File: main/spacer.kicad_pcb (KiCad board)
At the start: 2 copper layers, 100 x 100 mm, 114 parts

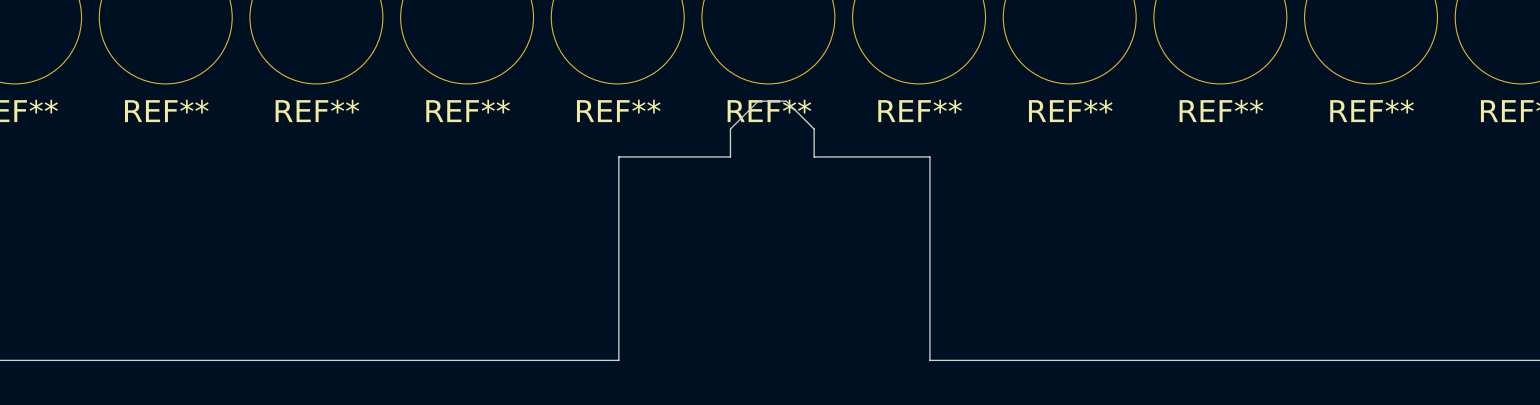
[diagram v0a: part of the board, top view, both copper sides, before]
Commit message: progress and yet not.  trying for v0.2.0, but some issues: letters not aligned, switches to tall, minute leds too close to USB_C
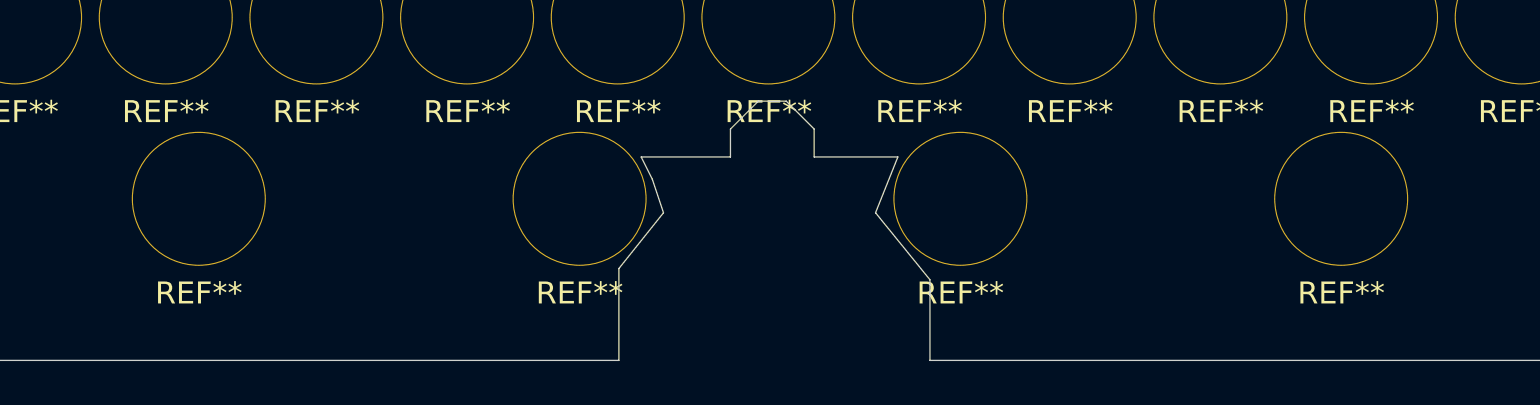
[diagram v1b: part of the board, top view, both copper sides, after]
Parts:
- added REF**: ws2812b-mini_hole, william_fab:ws2812b-mini_hole, F.Cu at (76.0, 92.6)
- added REF**: ws2812b-mini_hole, william_fab:ws2812b-mini_hole, F.Cu at (58.7, 92.6)
- added REF**: ws2812b-mini_hole, william_fab:ws2812b-mini_hole, F.Cu at (41.3, 92.6)
- added REF**: ws2812b-mini_hole, william_fab:ws2812b-mini_hole, F.Cu at (24.0, 92.6)
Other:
- outline, holes or cut-outs redrawn
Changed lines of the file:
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@@
-(kicad_pcb (version 20171130) (host pcbnew "(5.1.4)-1")
+(kicad_pcb (version 20171130) (host pcbnew "(5.1.5)-2")
   (general
     (thickness 1.6)
-    (drawings 47)
+    (drawings 52)
     (tracks 0)
     (zones 0)
-    (modules 114)
+    (modules 118)
     (nets 1)
   )
@@
       (drillshape 0)
       (scaleselection 1)
-      (outputdirectory "../fabrication/v0.2.0/"))
+      (outputdirectory "../fabrication/v0.2.0_spacer/"))
   )
   (net 0 "")
@@
   )
   (module william_fab:ws2812b-mini_hole (layer F.Cu)
+    (at 76 92.645)
+    (fp_text reference REF** (at 0 4.3) (layer F.SilkS)
+      (effects (font (size 1 1) (thickness 0.15)))
+    )
+    (fp_text value ws2812b-mini_hole (at 0.3 -6.35) (layer F.Fab)
+      (effects (font (size 1 1) (thickness 0.15)))
+    )
+    (pad 1 thru_hole circle (at 0 0) (size 6.1 6.1) (drill 6) (layers *.Cu *.Mask))
+  )
+  (module william_fab:ws2812b-mini_hole (layer F.Cu)
+    (at 58.666666 92.645)
+    (fp_text reference REF** (at 0 4.3) (layer F.SilkS)
+      (effects (font (size 1 1) (thickness 0.15)))
+    )
+    (fp_text value ws2812b-mini_hole (at 0.3 -6.35) (layer F.Fab)
+      (effects (font (size 1 1) (thickness 0.15)))
+    )
+    (pad 1 thru_hole circle (at 0 0) (size 6.1 6.1) (drill 6) (layers *.Cu *.Mask))
+  )
+  (module william_fab:ws2812b-mini_hole (layer F.Cu)
+    (at 41.333333 92.645)
+    (fp_text reference REF** (at 0 4.3) (layer F.SilkS)
+      (effects (font (size 1 1) (thickness 0.15)))
+    )
+    (fp_text value ws2812b-mini_hole (at 0.3 -6.35) (layer F.Fab)
+      (effects (font (size 1 1) (thickness 0.15)))
+    )
+    (pad 1 thru_hole circle (at 0 0) (size 6.1 6.1) (drill 6) (layers *.Cu *.Mask))
+  )
+  (module william_fab:ws2812b-mini_hole (layer F.Cu)
+    (at 24 92.645)
+    (fp_text reference REF** (at 0 4.3) (layer F.SilkS)
+      (effects (font (size 1 1) (thickness 0.15)))
+    )
+    (fp_text value ws2812b-mini_hole (at 0.3 -6.35) (layer F.Fab)
+      (effects (font (size 1 1) (thickness 0.15)))
+    )
+    (pad 1 thru_hole circle (at 0 0) (size 6.1 6.1) (drill 6) (layers *.Cu *.Mask))
+  )
+  (module william_fab:ws2812b-mini_hole (layer F.Cu)
     (at 84.2172 84.39)
     (fp_text reference REF** (at 0 4.3) (layer F.SilkS)
@@
     (pad "" np_thru_hole circle (at 0 0) (size 2.1 2.1) (drill 2.1) (layers *.Cu *.Mask))
   )
+  (gr_line (start 54.804 93.28) (end 57.2805 96.328) (layer Edge.Cuts) (width 0.05))
+  (gr_line (start 55.82 90.74) (end 54.804 93.28) (layer Edge.Cuts) (width 0.05))
+  (gr_line (start 45.152 93.28) (end 43.12 95.82) (layer Edge.Cuts) (width 0.05))
+  (gr_line (start 44.644 91.756) (end 45.152 93.28) (layer Edge.Cuts) (width 0.05))
+  (gr_line (start 44.136 90.74) (end 44.644 91.756) (layer Edge.Cuts) (width 0.05))
   (dimension 7.62 (width 0.13) (layer Cmts.User)
     (gr_text "7.620 mm" (at -13.3351 14.7432 270) (layer Cmts.User)
@@
   (gr_line (start 5 90) (end 5 85) (layer Edge.Cuts) (width 0.05))
   (gr_line (start 0 90) (end 5 90) (layer Edge.Cuts) (width 0.05))
-  (gr_line (start 52.01 90.74) (end 57.2805 90.74) (layer Edge.Cuts) (width 0.05))
+  (gr_line (start 52.01 90.74) (end 55.82 90.74) (layer Edge.Cuts) (width 0.05))
   (gr_line (start 52.01 89.47) (end 52.01 90.74) (layer Edge.Cuts) (width 0.05))
   (gr_line (start 50.74 88.2) (end 52.01 89.47) (layer Edge.Cuts) (width 0.05))
@@
   (gr_line (start 48.2 89.47) (end 49.47 88.2) (layer Edge.Cuts) (width 0.05))
   (gr_line (start 48.2 90.74) (end 48.2 89.47) (layer Edge.Cuts) (width 0.05))
-  (gr_line (start 43.12 90.74) (end 48.2 90.74) (layer Edge.Cuts) (width 0.05))
+  (gr_line (start 44.136 90.74) (end 48.2 90.74) (layer Edge.Cuts) (width 0.05))
   (gr_line (start 57.2805 100) (end 100 100) (layer Edge.Cuts) (width 0.05))
   (gr_line (start 0 100) (end 43.12 100) (layer Edge.Cuts) (width 0.05))
-  (gr_line (start 57.2805 90.74) (end 57.2805 100) (layer Edge.Cuts) (width 0.05))
-  (gr_line (start 43.12 100) (end 43.12 90.74) (layer Edge.Cuts) (width 0.05))
+  (gr_line (start 57.2805 96.328) (end 57.2805 100) (layer Edge.Cuts) (width 0.05))
+  (gr_line (start 43.12 100) (end 43.12 95.82) (layer Edge.Cuts) (width 0.05))
   (gr_line (start 100 0) (end 100 100) (layer Edge.Cuts) (width 0.05))
   (gr_line (start 0 0) (end 100 0) (layer Edge.Cuts) (width 0.05))
